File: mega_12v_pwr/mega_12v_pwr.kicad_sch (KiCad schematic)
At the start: 48 parts, among them J1 Conn_01x01, J10 Conn_01x01, J11 Conn_01x01, J12 Conn_01x01, J13 Conn_01x01, J14 Conn_01x01, J15 Conn_01x01, J16 Conn_01x01, J17 Conn_01x01, J18 Conn_01x01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

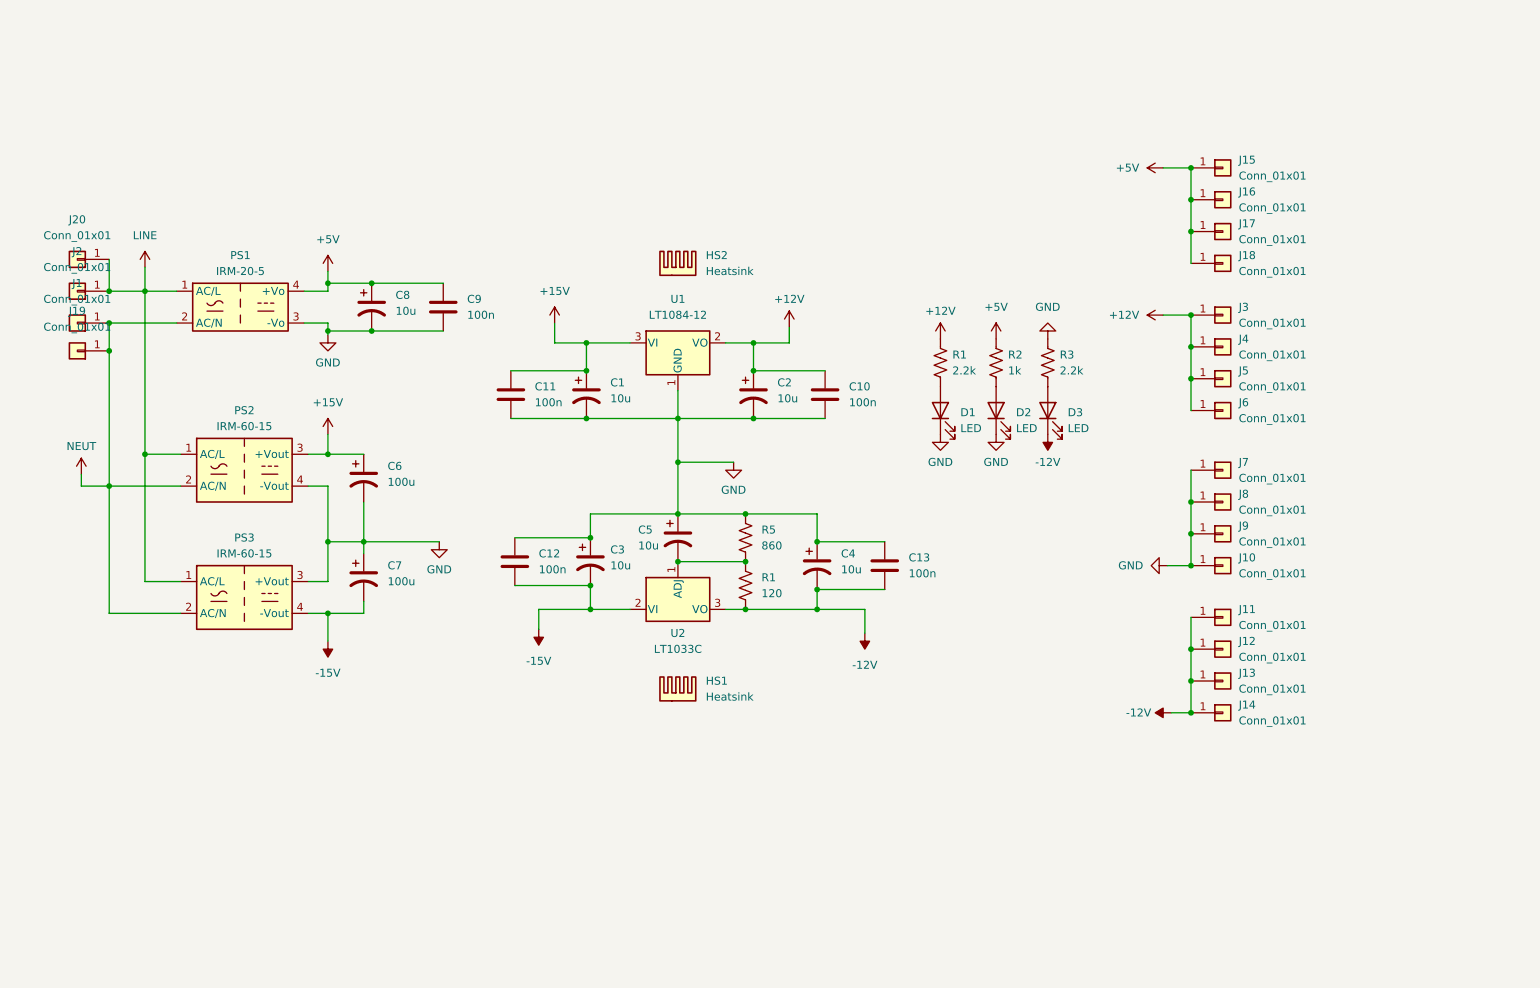
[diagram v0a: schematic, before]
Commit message: Added fan connector
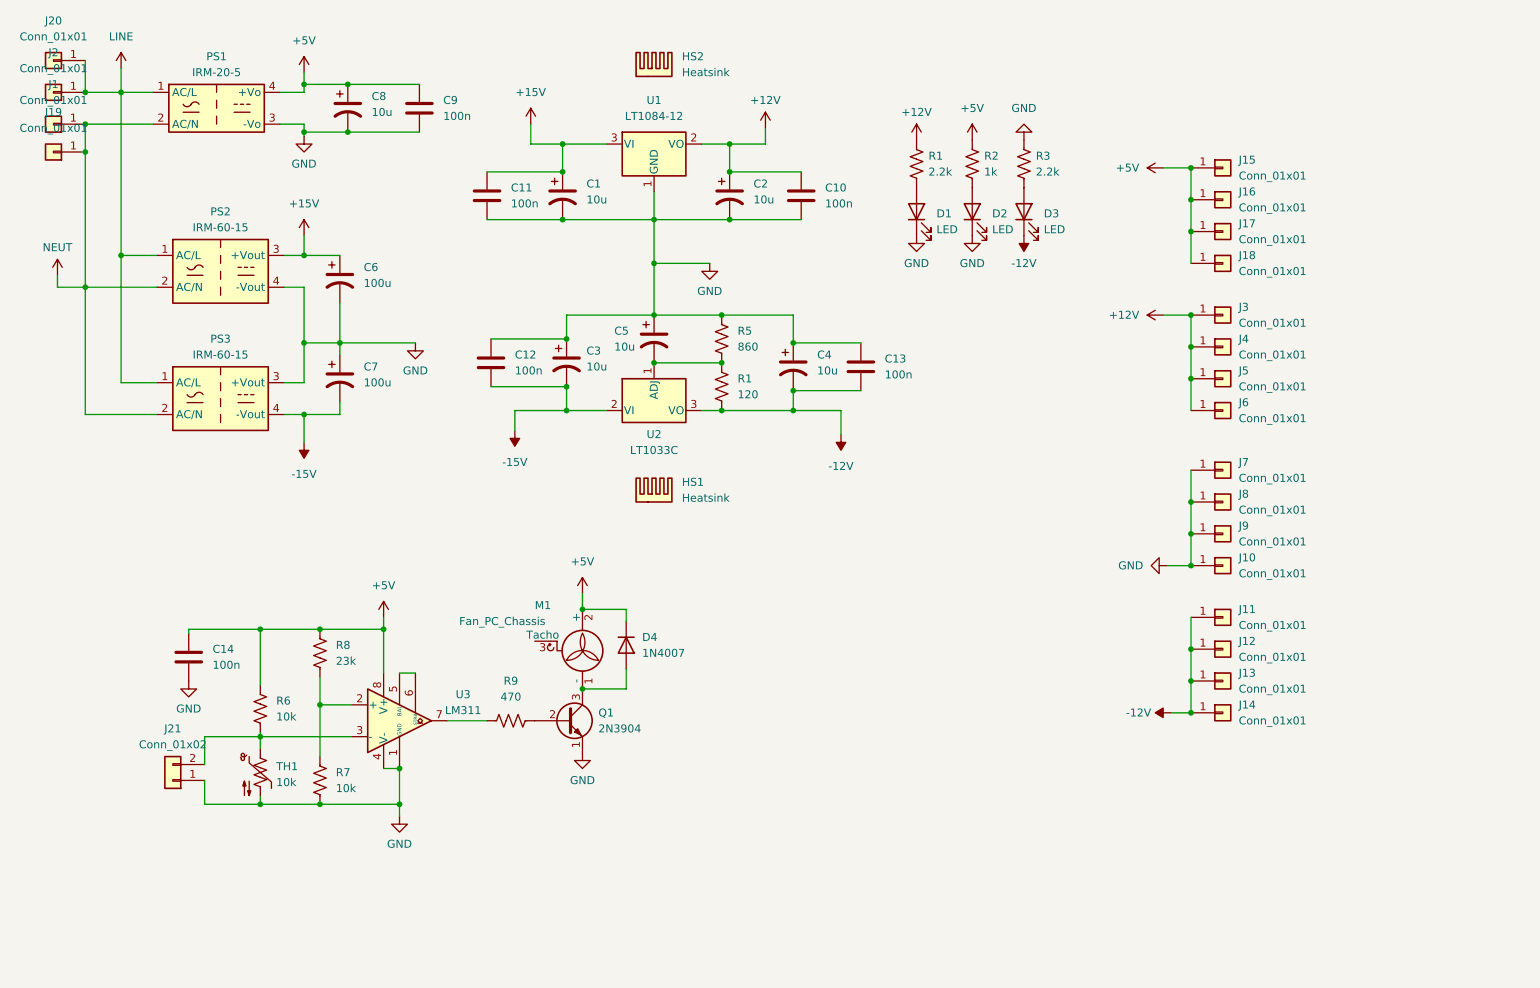
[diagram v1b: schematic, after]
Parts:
- added C14: 100n, Capacitor_THT:C_Disc_D6.0mm_W2.5mm_P5.00mm, symbol Device:C
- added D4: 1N4007, Diode_THT:D_DO-41_SOD81_P10.16mm_Horizontal, symbol Diode:1N4007
- added J21: Conn_01x02, Connector_PinHeader_2.54mm:PinHeader_1x02_P2.54mm_Vertical, symbol Connector_Generic:Conn_01x02
- added M1: Fan_PC_Chassis, Connector:FanPinHeader_1x03_P2.54mm_Vertical, symbol Motor:Fan_PC_Chassis
- added Q1: 2N3904, Package_TO_SOT_THT:TO-92_HandSolder, symbol Transistor_BJT:2N3904
- added R6, R7: 10k, Resistor_THT:R_Axial_DIN0207_L6.3mm_D2.5mm_P7.62mm_Horizontal, symbol Device:R_US
- added R8: 23k, Resistor_THT:R_Axial_DIN0207_L6.3mm_D2.5mm_P7.62mm_Horizontal, symbol Device:R_US
- added R9: 470, Resistor_THT:R_Axial_DIN0207_L6.3mm_D2.5mm_P7.62mm_Horizontal, symbol Device:R_US
- added TH1: 10k, Resistor_THT:R_Axial_DIN0204_L3.6mm_D1.6mm_P1.90mm_Vertical, symbol Device:Thermistor_NTC_US
- added U3: LM311, Package_DIP:DIP-8_W7.62mm, symbol Comparator:LM311
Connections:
- net +5V: now also C14.1, D4.1 (K), M1.2 (+), R6.1, R8.1, U3.8 (V+)
- net GND: now also C14.2, J21.1 (Pin_1), Q1.1 (E), R7.2, TH1.2, U3.1 (GND), U3.4 (V-)
- new net: J21.2 (Pin_2), R6.2, TH1.1, U3.3 (-)
- new net: R7.1, R8.2, U3.2 (+)
- new net: U3.5 (BAL), U3.6 (STRB)
- new net: R9.1, U3.7
- new net: D4.2 (A), M1.1 (-), Q1.3 (C)
- new net: Q1.2 (B), R9.2
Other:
- moved on the sheet: C1, C10, C11, C12, C13, C2, C3, C4, C5, C6, C7, C8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

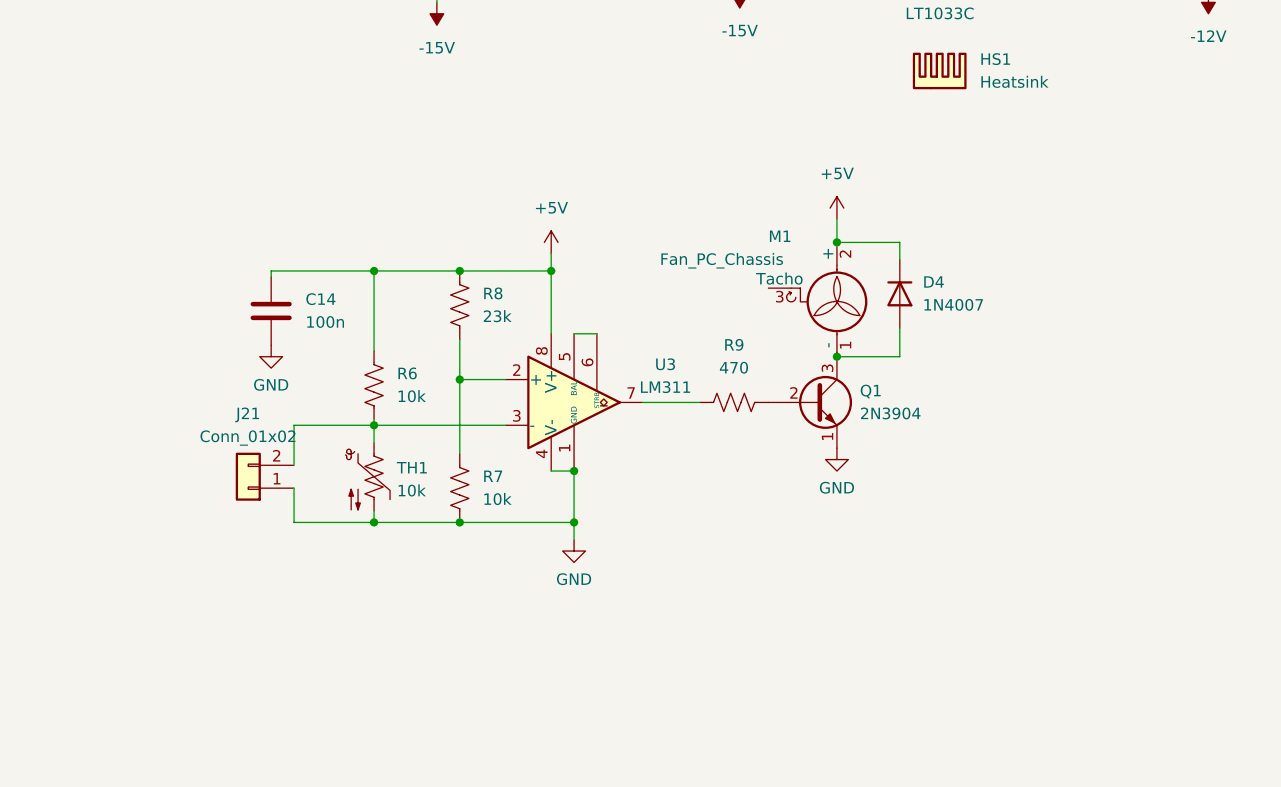
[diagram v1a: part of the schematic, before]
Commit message: Switched to PWM fan controller
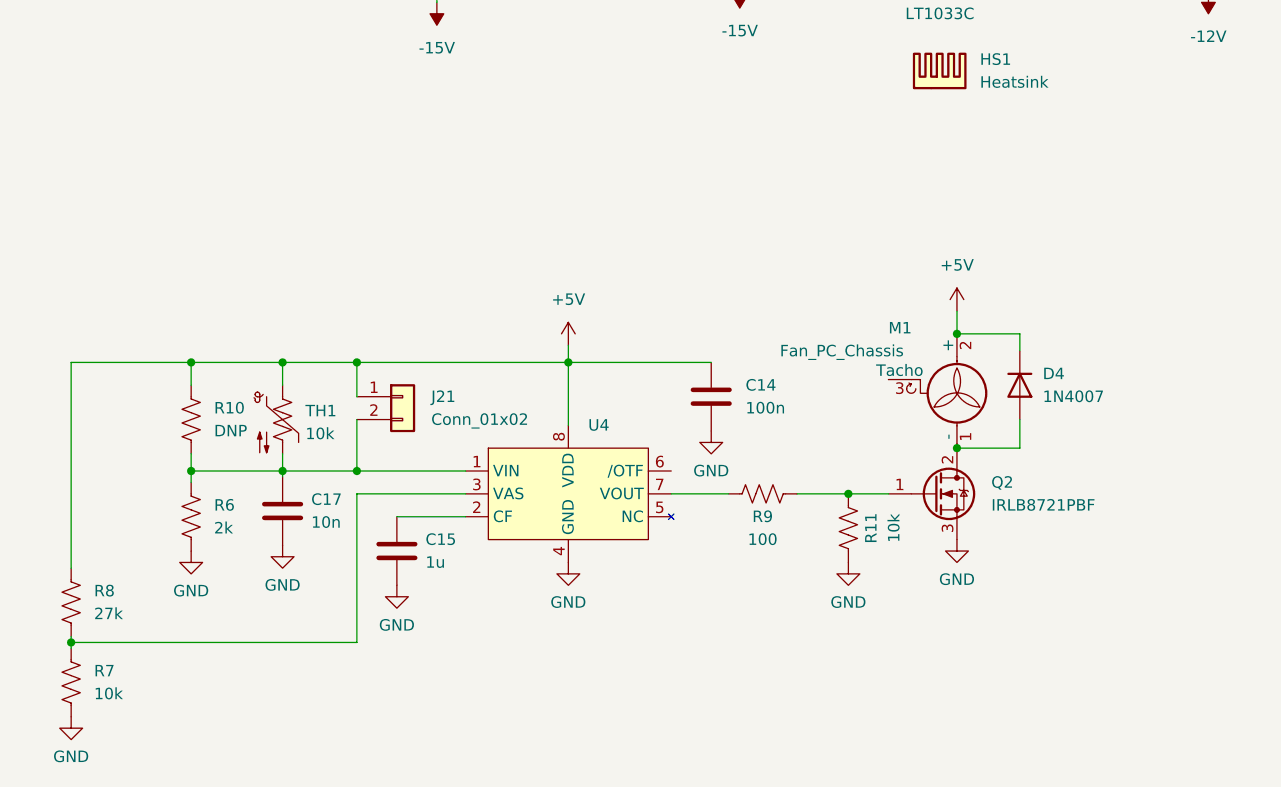
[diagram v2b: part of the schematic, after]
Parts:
- removed Q1: 2N3904, Package_TO_SOT_THT:TO-92_HandSolder, symbol Transistor_BJT:2N3904
- removed U3: LM311, Package_DIP:DIP-8_W7.62mm, symbol Comparator:LM311
- added C15: 1u, Capacitor_THT:C_Disc_D6.0mm_W2.5mm_P5.00mm, symbol Device:C
- added C17: 10n, Capacitor_THT:C_Disc_D6.0mm_W2.5mm_P5.00mm, symbol Device:C
- added Q2: IRLB8721PBF, Package_TO_SOT_THT:TO-220-3_Vertical, symbol Transistor_FET:IRLB8721PBF
- added R10: DNP, Resistor_THT:R_Axial_DIN0207_L6.3mm_D2.5mm_P7.62mm_Horizontal, symbol Device:R_US
- added R11: 10k, Resistor_THT:R_Axial_DIN0207_L6.3mm_D2.5mm_P7.62mm_Horizontal, symbol Device:R_US
- added U4: ~, Package_DIP:DIP-8_W7.62mm, symbol Alex_Custom:TC648
- R6: value 10k -> 2k
- R8: value 23k -> 27k
- R9: value 470 -> 100
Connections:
- net +5V: now also J21.1 (Pin_1), TH1.1, R10.1, U4.8 (VDD); no longer R6.1
- net GND: now also R6.2, C15.2, C17.2, Q2.3 (S), R11.1, U4.4 (GND); no longer J21.1 (Pin_1), TH1.2
- net at R7.1, R8.2: now also U4.3 (VAS)
- net at R9.1: now also U4.7 (VOUT)
- net at D4.2 (A), M1.1 (-): now also Q2.2 (D)
- net at R9.2: now also Q2.1 (G), R11.2
- new net: C17.1, J21.2 (Pin_2), R10.2, R6.1, TH1.2, U4.1 (VIN)
- new net: C15.1, U4.2 (CF)
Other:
- moved on the sheet: C14, D4, J21, M1, R7, R8, R9, TH1

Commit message: Added more ground terminals
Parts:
- added J22, J23, J24, J25: Conn_01x01, AlexCustom:SPADE, symbol Connector_Generic:Conn_01x01
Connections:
- net GND: now also J22.1 (Pin_1), J23.1 (Pin_1), J24.1 (Pin_1), J25.1 (Pin_1)
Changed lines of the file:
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@@
   (junction (at 156.21 78.105) (diameter 0) (color 0 0 0 0)
   )
+  (junction (at 252.73 104.14) (diameter 0) (color 0 0 0 0)
+  )
   (junction (at 120.015 88.9) (diameter 0) (color 0 0 0 0)
   )
   (junction (at 78.105 78.105) (diameter 0) (color 0 0 0 0)
   )
+  (junction (at 252.73 109.22) (diameter 0) (color 0 0 0 0)
+  )
   (junction (at 219.71 113.665) (diameter 0) (color 0 0 0 0)
   )
@@
   (junction (at 146.05 50.8) (diameter 0) (color 0 0 0 0)
   )
+  (junction (at 252.73 114.3) (diameter 0) (color 0 0 0 0)
+  )
   (junction (at 50.8 146.05) (diameter 0) (color 0 0 0 0)
   )
@@
     (stroke (width 0) (type default))
   )
+  (wire (pts (xy 248.92 114.3) (xy 252.73 114.3))
+    (stroke (width 0) (type default))
+  )
   (wire (pts (xy 50.8 147.32) (xy 50.8 146.05))
     (stroke (width 0) (type default))
@@
     (stroke (width 0) (type default))
   )
+  (wire (pts (xy 252.73 109.22) (xy 252.73 114.3))
+    (stroke (width 0) (type default))
+  )
   (wire (pts (xy 43.18 33.02) (xy 43.18 38.1))
     (stroke (width 0) (type default))
@@
     (stroke (width 0) (type default))
   )
+  (wire (pts (xy 252.73 99.06) (xy 252.73 104.14))
+    (stroke (width 0) (type default))
+  )
   (wire (pts (xy 60.96 133.985) (xy 50.8 133.985))
     (stroke (width 0) (type default))
@@
     (stroke (width 0) (type default))
   )
+  (wire (pts (xy 252.73 104.14) (xy 252.73 109.22))
+    (stroke (width 0) (type default))
+  )
   (wire (pts (xy 43.18 47.625) (xy 43.18 43.18))
     (stroke (width 0) (type default))
@@
         (path "/a540ca66-0b58-4779-9c5f-095a0955b41b"
           (reference "J6") (unit 1)
+        )
+      )
+    )
+  )
+  (symbol (lib_id "power:GND") (at 248.92 114.3 270) (unit 1)
+    (in_bom yes) (on_board yes) (dnp no) (fields_autoplaced)
+    (property "Reference" "#PWR027" (at 242.57 114.3 0)
+      (effects (font (size 1.27 1.27)) hide)
+    )
+    (property "Value" "GND" (at 245.11 114.3 90)
+      (effects (font (size 1.27 1.27)) (justify right))
+    )
+    (property "Footprint" "" (at 248.92 114.3 0)
+      (effects (font (size 1.27 1.27)) hide)
+    )
+    (property "Datasheet" "" (at 248.92 114.3 0)
+      (effects (font (size 1.27 1.27)) hide)
+    )
+    (pin "1")
+    (instances
+      (project "mega_12v_pwr"
+        (path "/a540ca66-0b58-4779-9c5f-095a0955b41b"
+          (reference "#PWR027") (unit 1)
+        )
+      )
+    )
+  )
+  (symbol (lib_id "Connector_Generic:Conn_01x01") (at 257.81 109.22 0) (unit 1)
+    (in_bom yes) (on_board yes) (dnp no) (fields_autoplaced)
+    (property "Reference" "J24" (at 260.35 107.95 0)
+      (effects (font (size 1.27 1.27)) (justify left))
+    )
+    (property "Value" "Conn_01x01" (at 260.35 110.49 0)
+      (effects (font (size 1.27 1.27)) (justify left))
+    )
+    (property "Footprint" "AlexCustom:SPADE" (at 257.81 109.22 0)
+      (effects (font (size 1.27 1.27)) hide)
+    )
+    (property "Datasheet" "~" (at 257.81 109.22 0)
+      (effects (font (size 1.27 1.27)) hide)
+    )
+    (pin "1")
+    (instances
+      (project "mega_12v_pwr"
+        (path "/a540ca66-0b58-4779-9c5f-095a0955b41b"
+          (reference "J24") (unit 1)
         )
       )
@@
     )
   )
+  (symbol (lib_id "Connector_Generic:Conn_01x01") (at 257.81 104.14 0) (unit 1)
+    (in_bom yes) (on_board yes) (dnp no) (fields_autoplaced)
+    (property "Reference" "J23" (at 260.35 102.87 0)
+      (effects (font (size 1.27 1.27)) (justify left))
+    )
+    (property "Value" "Conn_01x01" (at 260.35 105.41 0)
+      (effects (font (size 1.27 1.27)) (justify left))
+    )
+    (property "Footprint" "AlexCustom:SPADE" (at 257.81 104.14 0)
+      (effects (font (size 1.27 1.27)) hide)
+    )
+    (property "Datasheet" "~" (at 257.81 104.14 0)
+      (effects (font (size 1.27 1.27)) hide)
+    )
+    (pin "1")
+    (instances
+      (project "mega_12v_pwr"
+        (path "/a540ca66-0b58-4779-9c5f-095a0955b41b"
+          (reference "J23") (unit 1)
+        )
+      )
+    )
+  )
   (symbol (lib_id "Connector_Generic:Conn_01x02") (at 74.295 137.795 0) (unit 1)
     (in_bom yes) (on_board yes) (dnp no) (fields_autoplaced)
@@
     )
   )
+  (symbol (lib_id "Connector_Generic:Conn_01x01") (at 257.81 114.3 0) (unit 1)
+    (in_bom yes) (on_board yes) (dnp no) (fields_autoplaced)
+    (property "Reference" "J25" (at 260.35 113.03 0)
+      (effects (font (size 1.27 1.27)) (justify left))
+    )
+    (property "Value" "Conn_01x01" (at 260.35 115.57 0)
+      (effects (font (size 1.27 1.27)) (justify left))
+    )
+    (property "Footprint" "AlexCustom:SPADE" (at 257.81 114.3 0)
+      (effects (font (size 1.27 1.27)) hide)
+    )
+    (property "Datasheet" "~" (at 257.81 114.3 0)
+      (effects (font (size 1.27 1.27)) hide)
+    )
+    (pin "1")
+    (instances
+      (project "mega_12v_pwr"
+        (path "/a540ca66-0b58-4779-9c5f-095a0955b41b"
+          (reference "J25") (unit 1)
+        )
+      )
+    )
+  )
   (symbol (lib_id "Connector_Generic:Conn_01x01") (at 224.79 60.325 0) (unit 1)
     (in_bom yes) (on_board yes) (dnp no) (fields_autoplaced)
@@
         )
       )
+    )
+  )
+  (symbol (lib_id "Connector_Generic:Conn_01x01") (at 257.81 99.06 0) (unit 1)
+    (in_bom yes) (on_board yes) (dnp no) (fields_autoplaced)
+    (property "Reference" "J22" (at 260.35 97.79 0)
+      (effects (font (size 1.27 1.27)) (justify left))
+    )
+    (property "Value" "Conn_01x01" (at 260.35 100.33 0)
+      (effects (font (size 1.27 1.27)) (justify left))
+    )
+    (property "Footprint" "AlexCustom:SPADE" (at 257.81 99.06 0)
+      (effects (font (size 1.27 1.27)) hide)
+    )
+    (property "Datasheet" "~" (at 257.81 99.06 0)
+      (effects (font (size 1.27 1.27)) hide)
+    )
+    (pin "1")
+    (instances
+      (project "mega_12v_pwr"
+        (path "/a540ca66-0b58-4779-9c5f-095a0955b41b"
+          (reference "J22") (unit 1)
+        )
+      )
